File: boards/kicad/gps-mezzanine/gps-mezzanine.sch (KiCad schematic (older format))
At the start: 36 parts, among them J1 USB_OTG, J2 CONN_02X06, J3 CONN_02X06, P1 CONN_02X20, U1 MCP1700T-3302E/TT, U2 FGPMMOPA6H, U3 TXS0104E, U4 FT230X, U5 MCP1700T-1802E

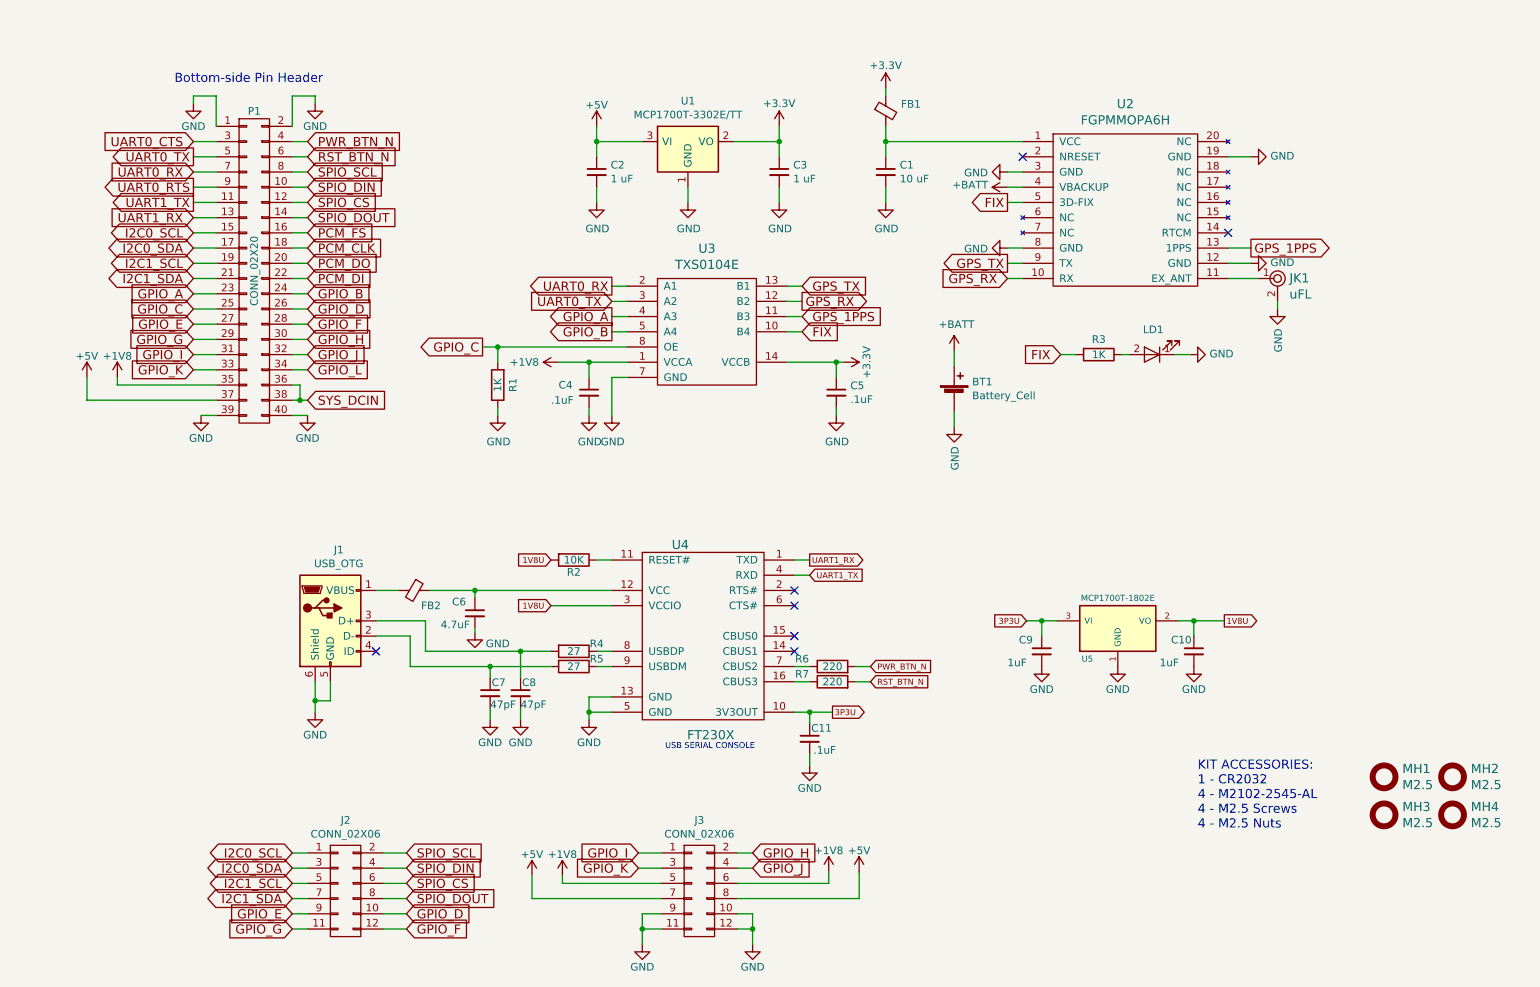
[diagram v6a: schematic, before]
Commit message: Updates for maufacturing
Adds fiducials for manufacturing.
Switches to SMT USB connector.
Fixes pattern for the level translator.
Adds QWERTY logo to the bottom of the board.

Signed-off-by: Michael Welling <mwelling@ieee.org>
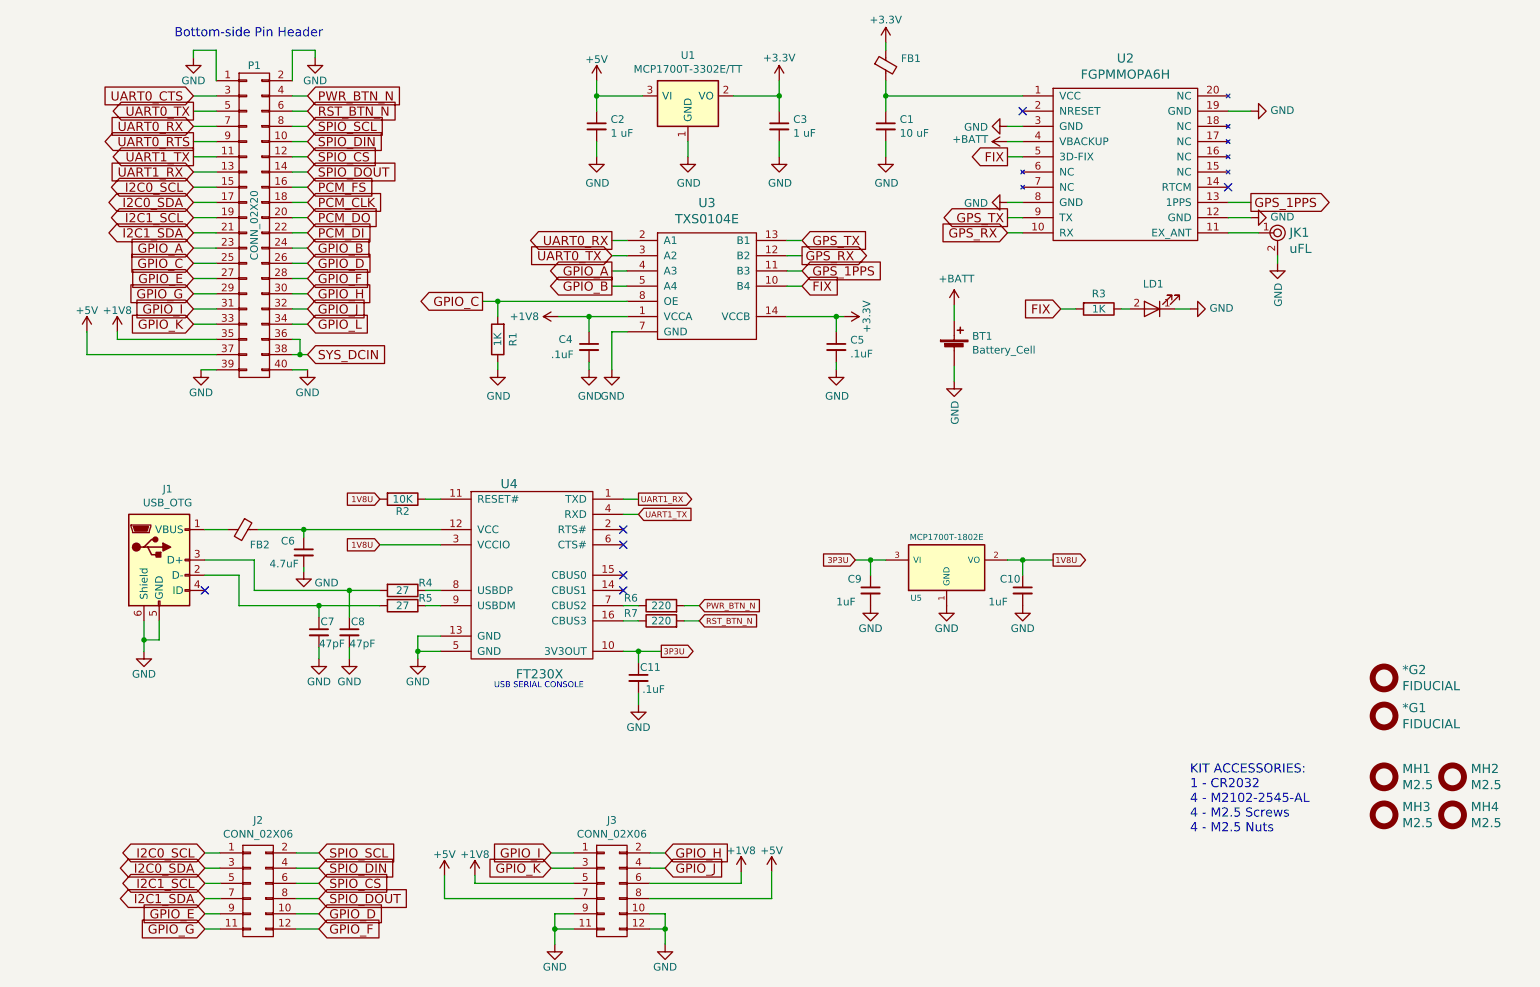
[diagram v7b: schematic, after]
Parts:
- added *G1, *G2: FIDUCIAL, 96boards:Fiducial_1mm_Dia_2.00mm_Outer_CopperTop, symbol MOUNTING_HOLE
- J1: footprint Connect:USB_Micro-B -> 96boards:10118192-0001LF(MICRO-USB-B-AMPHENOL-FCI); Mfg Part Number 10118194-0001LF -> 10118192-0001LF
- U3: footprint Housings_SSOP:SSOP-14_5.3x6.2mm_Pitch0.65mm -> 96boards:TSSOP-14_4.3x5.1mm_Pitch0.65mm
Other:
- moved on the sheet: BT1, C1, C10, C11, C2, C3, C4, C5, C6, C7, C8, C9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
